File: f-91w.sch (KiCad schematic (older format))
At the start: 38 parts, among them P10 CONN_01X01, P11 CONN_01X01, P13 CONN_01X01, P14 CONN_01X01, P5 CONN_01X01, P6 CONN_01X01, P7 CONN_01X01, P8 CONN_01X01, P9 CONN_01X01, Q1 BC846, U1 CY8C4248LQI-BL483, U2 LCD-F-91W, U3 BME680, Y1 32.768KHz, Y2 24MHz

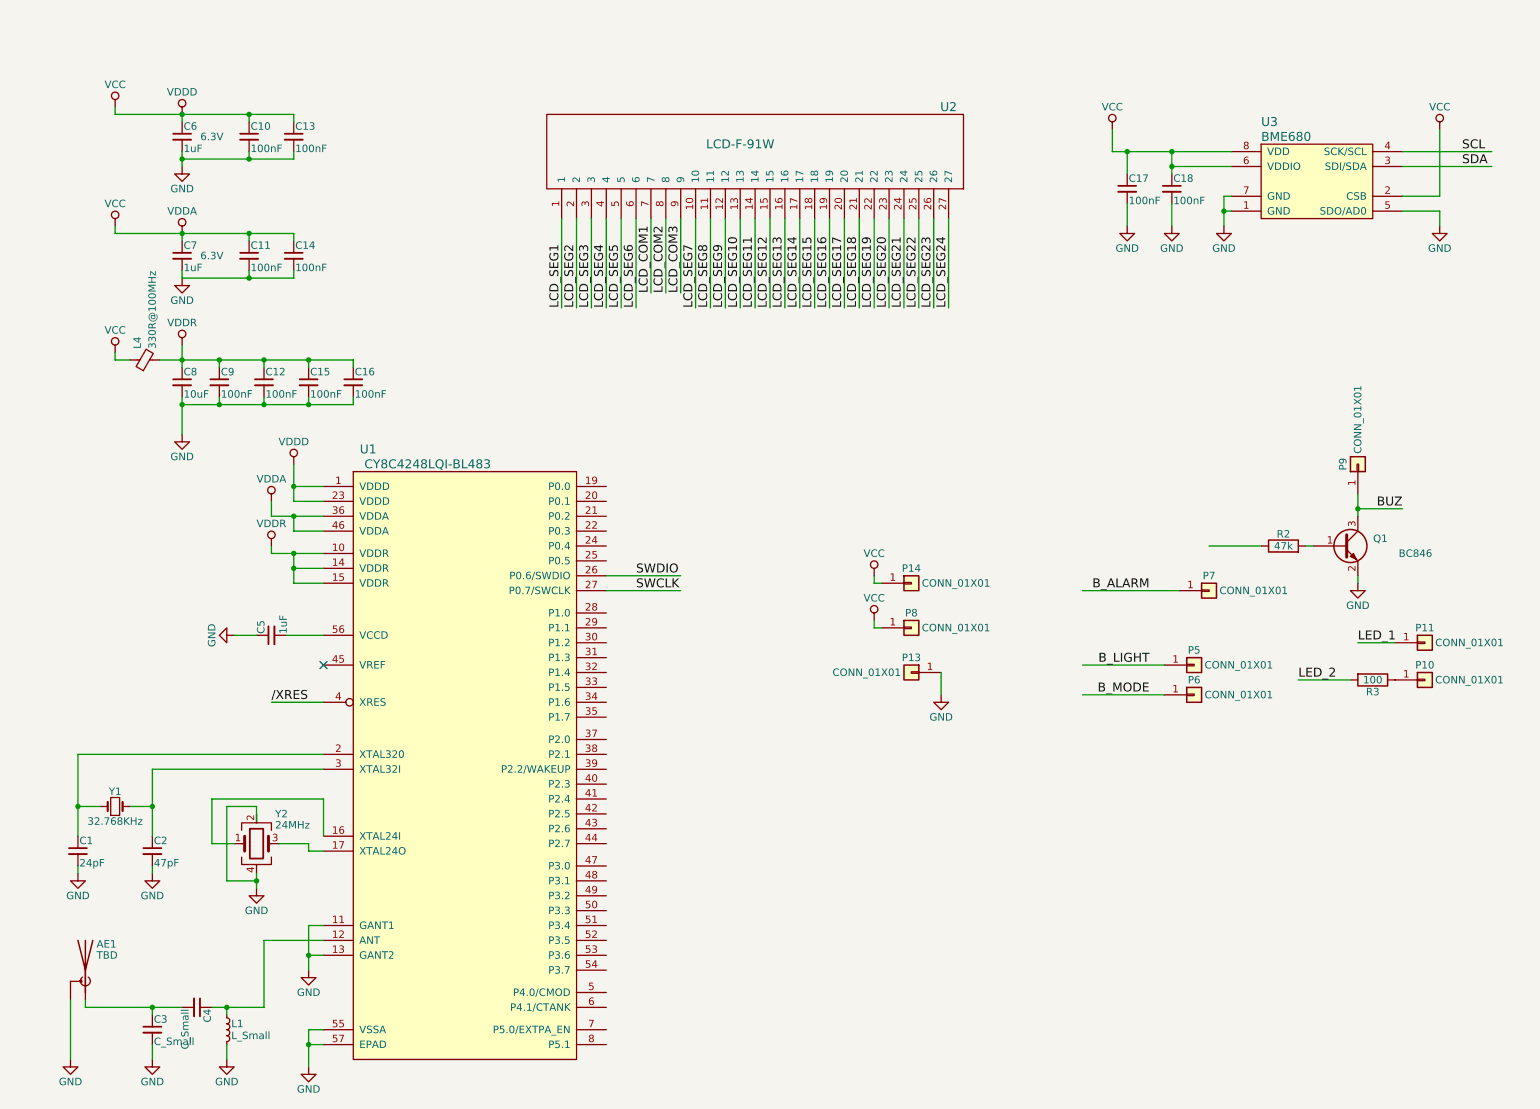
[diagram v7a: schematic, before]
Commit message: Fully connect schematic
Tested in PSoC creator, and seems routable.
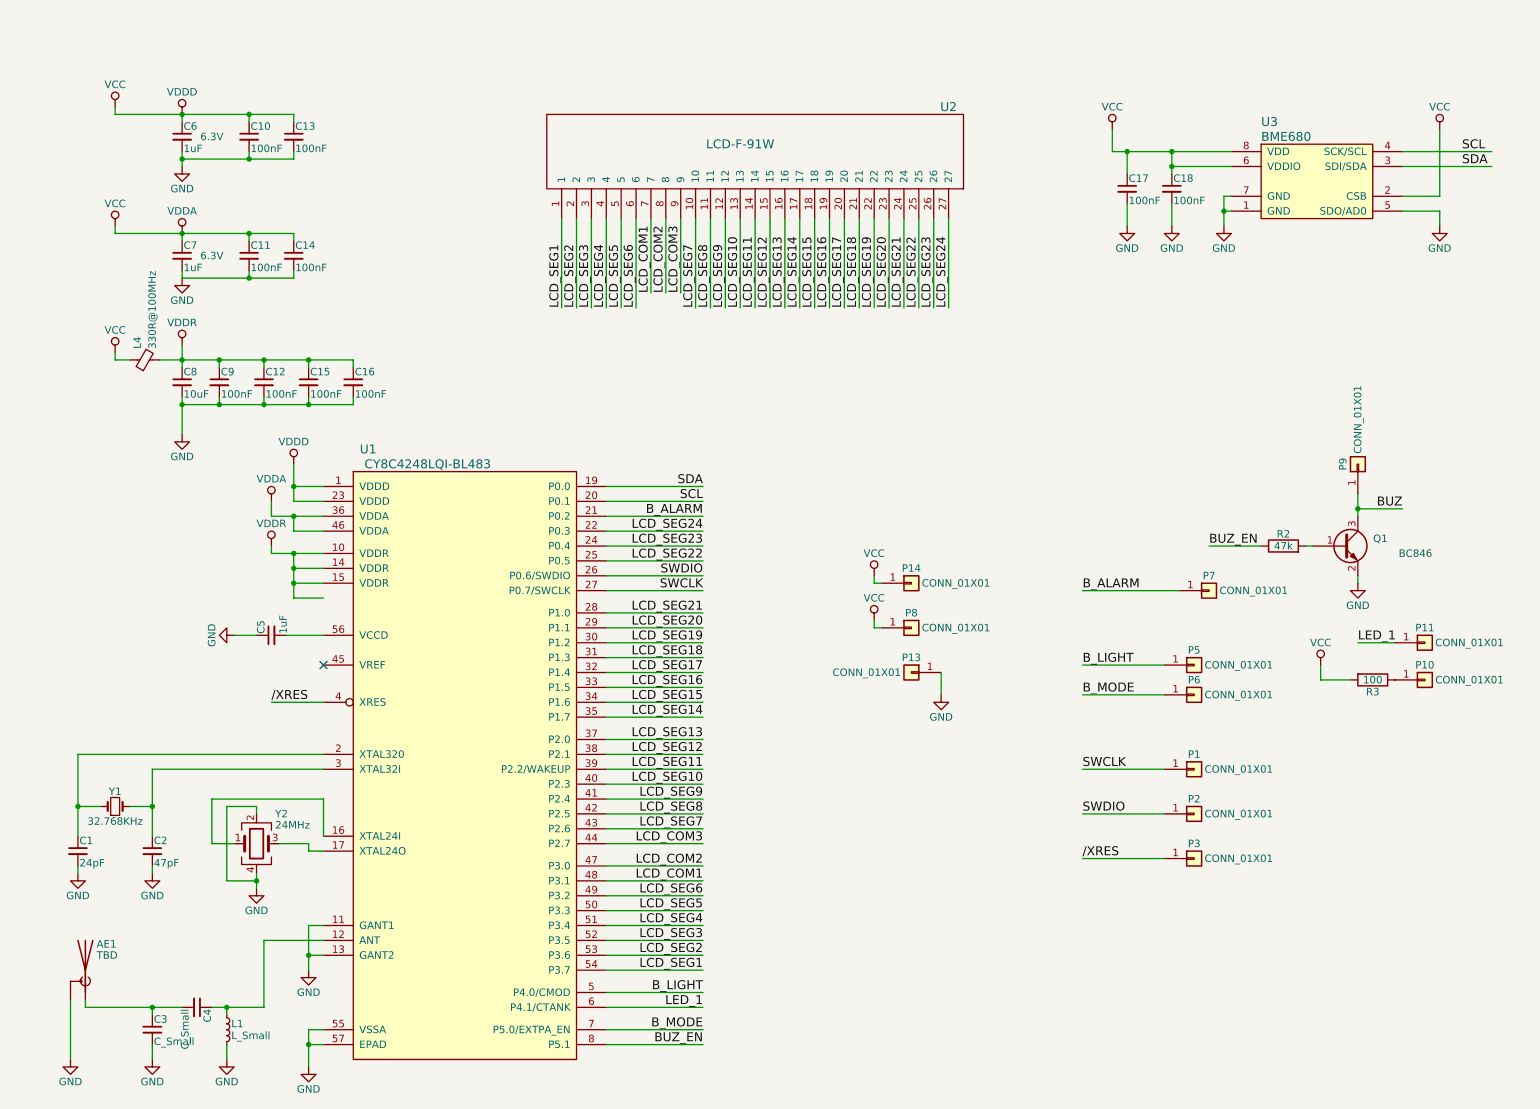
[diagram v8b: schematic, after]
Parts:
- added P1, P2, P3: CONN_01X01, symbol Conn_01x01
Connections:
- net labels added: BUZ_EN
- net labels removed: LED_2
- wire segments 143 -> 182
